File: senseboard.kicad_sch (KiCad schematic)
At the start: 73 parts, among them J1 Micro_SD_Card_Det1, J2 USB_C_Receptacle_USB2.0_16P, SW1 SW_Push, U1 STM32L4Q5CGUx, U2 SHT4x, U3 SCD41-D-R2, U4 SGP41-D-R4, U5 TPS62840DLCR, U6 TPS62840DLCR, U7 USBLC6-2SC6, U8 SGP41-D-R4, U9 RFM95W-915S2, Y1 Crystal_GND3

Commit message: added initial bom
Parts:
- U2: renamed from U6; footprint VSON8_2P1X1P6_TEX -> TPS62840DLCR:VSON8_2P1X1P6_TEX
- U3: renamed from U5; footprint VSON8_2P1X1P6_TEX -> TPS62840DLCR:VSON8_2P1X1P6_TEX
- renumbered C8 to C11, C11 to C12, C9 to C13, C7 to C14, C19 to C16, C20 to C17, C16 to C18, C21 to C19, C3 to C2, C22 to C20, C17 to C21, C23 to C22, C24 to C23, C18 to C24, C5 to C3, C13 to C4, C12 to C5, C2 to C6, C4 to C7, C14 to C8, C6 to C9, D3 to D1, D1 to D2, D4 to D3, D2 to D4, J2 to J1, J1 to J2, R2 to R1, R19 to R10, R20 to R11, R21 to R12, R5 to R13, R3 to R14, R22 to R15, R6 to R16, R7 to R17, R8 to R18, R9 to R19, R15 to R2, R10 to R20, R11 to R21, R12 to R22, R25 to R24, R24 to R25, R16 to R3, R13 to R4, R14 to R5, R1 to R6, R4 to R7, R17 to R8, R18 to R9, U7 to U1, U3 to U4, U4 to U5, U8 to U6, U2 to U7, U1 to U8

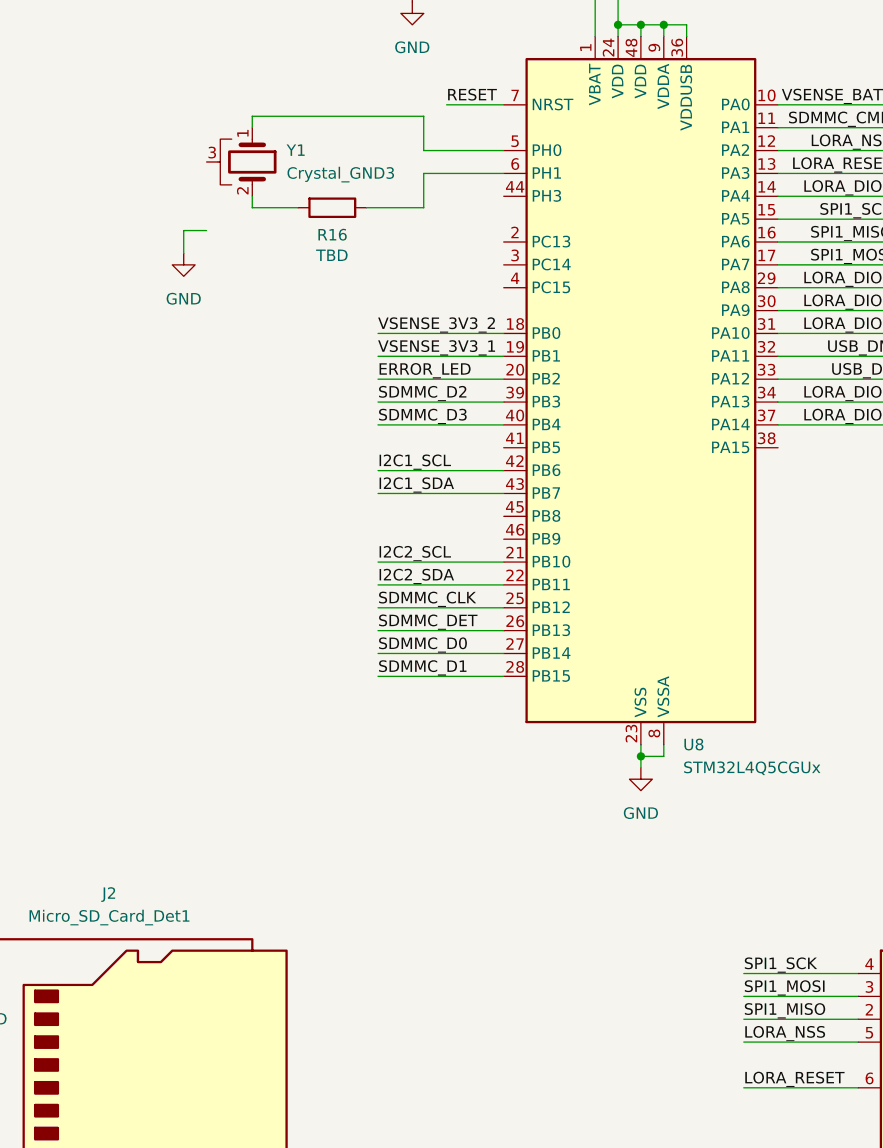
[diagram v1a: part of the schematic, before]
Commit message: fixed gnd positioning and added error led
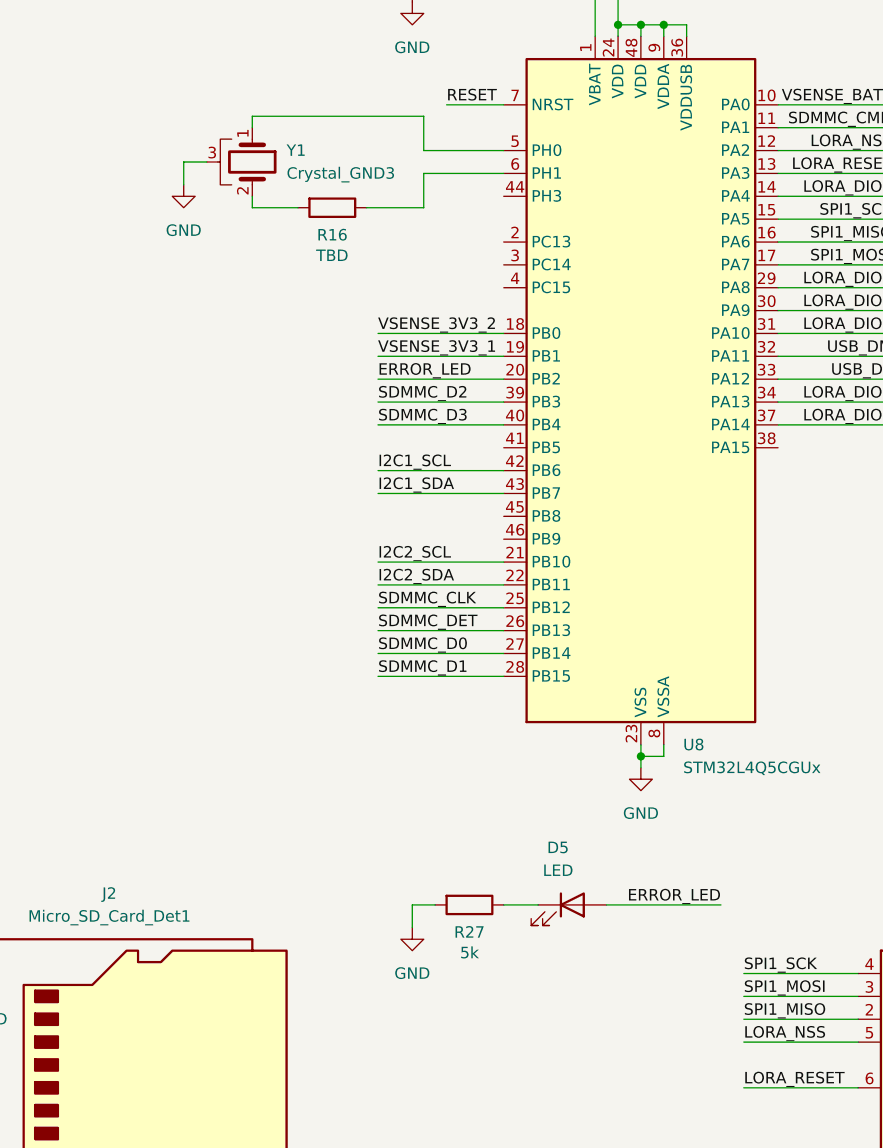
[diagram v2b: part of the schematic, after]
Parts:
- added D5: LED, symbol Device:LED
- added R27: 5k, symbol Device:R
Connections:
- net ERROR_LED: now also D5.2 (A)
- net GND: now also Y1.3, R27.2
- new net: D5.1 (K), R27.1

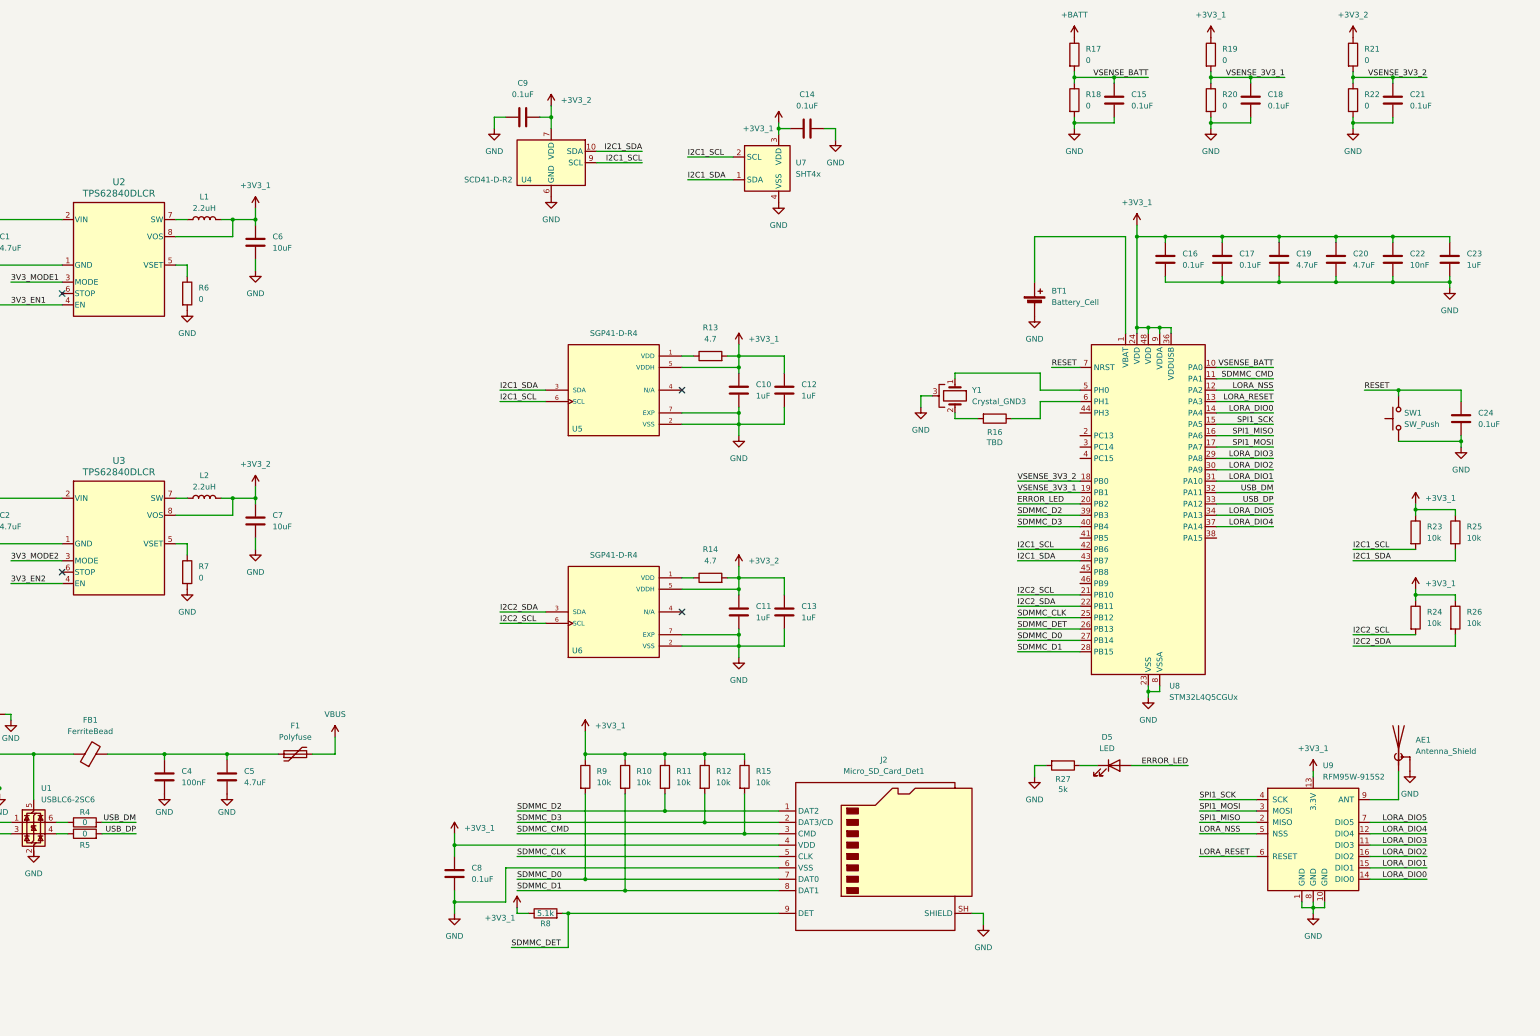
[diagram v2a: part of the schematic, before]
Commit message: minor changes to schematic, modified sd card holder and added all footprint references, began layout of board
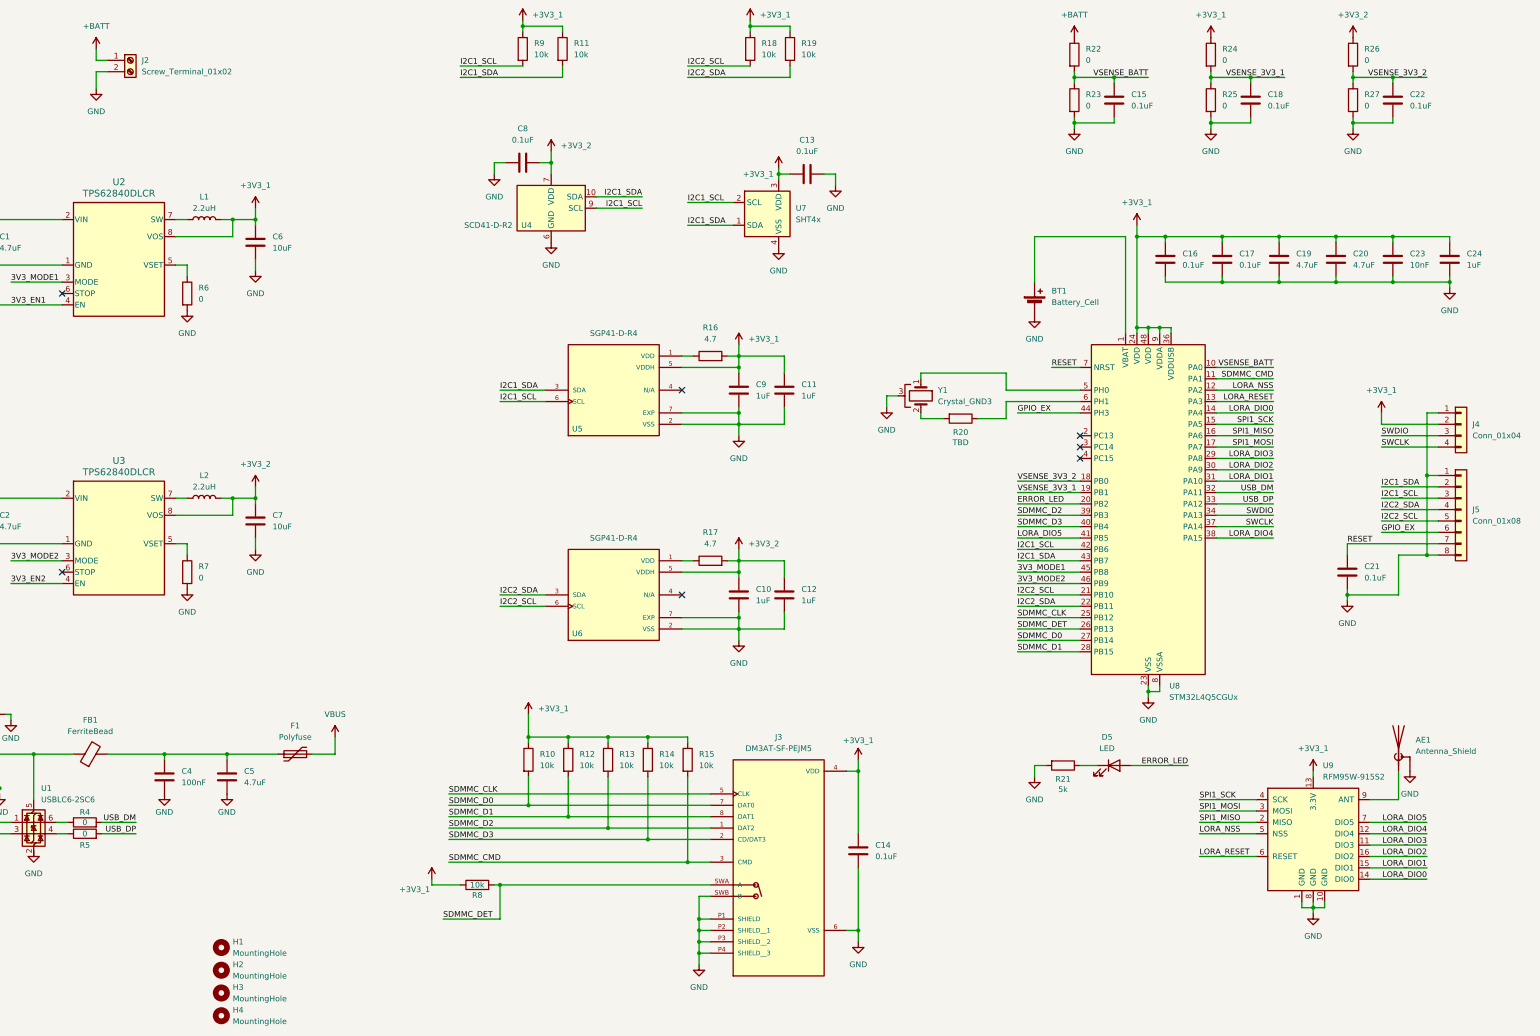
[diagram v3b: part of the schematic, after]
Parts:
- removed J2: Micro_SD_Card_Det1, symbol Connector:Micro_SD_Card_Det1
- removed SW1: SW_Push, symbol Switch:SW_Push
- added H1, H2, H3, H4: MountingHole, MountingHole:MountingHole_3.2mm_M3_ISO7380, symbol Mechanical:MountingHole
- added J2: Screw_Terminal_01x02, Connector_JST:JST_XH_B2B-XH-AM_1x02_P2.50mm_Vertical, symbol Connector:Screw_Terminal_01x02
- added J3: DM3AT-SF-PEJM5, DM3AT_SF_PEJM5:HRS_DM3AT-SF-PEJM5, symbol DM3AT-SF-PEJM5:DM3AT-SF-PEJM5
- added J4: Conn_01x04, Connector_PinHeader_2.54mm:PinHeader_1x04_P2.54mm_Vertical, symbol Connector_Generic:Conn_01x04
- added J5: Conn_01x08, Connector_PinHeader_2.54mm:PinHeader_1x08_P2.54mm_Vertical, symbol Connector_Generic:Conn_01x08
- AE1: footprint (none) -> Connector_Coaxial:SMA_Molex_73251-1153_EdgeMount_Horizontal
- BT1: footprint (none) -> Battery:BatteryHolder_Keystone_1057_1x2032
- C1, C19, C2, C20, C5, C6, C7: footprint (none) -> Capacitor_SMD:C_0805_2012Metric
- C10: renamed from C11; footprint (none) -> Capacitor_SMD:C_0603_1608Metric
- C11: renamed from C12; footprint (none) -> Capacitor_SMD:C_0603_1608Metric
- C12: renamed from C13; footprint (none) -> Capacitor_SMD:C_0603_1608Metric
- C13: renamed from C14; footprint (none) -> Capacitor_SMD:C_0402_1005Metric
- C14: renamed from C8; footprint (none) -> Capacitor_SMD:C_0402_1005Metric
- C15, C16, C17, C18, C3, C4: footprint (none) -> Capacitor_SMD:C_0402_1005Metric
- C21: renamed from C24; footprint (none) -> Capacitor_SMD:C_0402_1005Metric
- C22: renamed from C21; footprint (none) -> Capacitor_SMD:C_0402_1005Metric
- C23: renamed from C22; footprint (none) -> Capacitor_SMD:C_0402_1005Metric
- C24: renamed from C23; footprint (none) -> Capacitor_SMD:C_0603_1608Metric
- C8: renamed from C9; footprint (none) -> Capacitor_SMD:C_0402_1005Metric
- C9: renamed from C10; footprint (none) -> Capacitor_SMD:C_0603_1608Metric
- D1, D2, D3, D4: footprint (none) -> Diode_SMD:D_SMP_DO-220AA
- D5: footprint (none) -> LED_SMD:LED_0402_1005Metric
- F1: footprint (none) -> Fuse:Fuse_0805_2012Metric
- FB1: footprint (none) -> Inductor_SMD:L_0603_1608Metric
- J1: footprint (none) -> Connector_USB:USB_C_Receptacle_G-Switch_GT-USB-7010ASV
- L1, L2: footprint (none) -> Inductor_SMD:L_Murata_DFE201610P
- R1, R15, R2, R3, R4, R5, R6, R7: footprint (none) -> Resistor_SMD:R_0402_1005Metric
- R10: renamed from R9; footprint (none) -> Resistor_SMD:R_0402_1005Metric
- R11: renamed from R25; footprint (none) -> Resistor_SMD:R_0402_1005Metric
- R12: renamed from R10; footprint (none) -> Resistor_SMD:R_0402_1005Metric
- R13: renamed from R11; footprint (none) -> Resistor_SMD:R_0402_1005Metric
- R14: renamed from R12; footprint (none) -> Resistor_SMD:R_0402_1005Metric
- R16: renamed from R13; footprint (none) -> Resistor_SMD:R_0603_1608Metric
- R17: renamed from R14; footprint (none) -> Resistor_SMD:R_0603_1608Metric
- R18: renamed from R24; footprint (none) -> Resistor_SMD:R_0402_1005Metric
- R19: renamed from R26; footprint (none) -> Resistor_SMD:R_0402_1005Metric
- R20: renamed from R16; footprint (none) -> Resistor_SMD:R_0402_1005Metric
- R21: renamed from R27; footprint (none) -> Resistor_SMD:R_0402_1005Metric
- R22: renamed from R17; footprint (none) -> Resistor_SMD:R_0402_1005Metric
- R23: renamed from R18; footprint (none) -> Resistor_SMD:R_0402_1005Metric
- R24: renamed from R19; footprint (none) -> Resistor_SMD:R_0402_1005Metric
- R25: renamed from R20; footprint (none) -> Resistor_SMD:R_0402_1005Metric
- R26: renamed from R21; footprint (none) -> Resistor_SMD:R_0402_1005Metric
- R27: renamed from R22; footprint (none) -> Resistor_SMD:R_0402_1005Metric
- R8: value 5.1k -> 10k; footprint (none) -> Resistor_SMD:R_0402_1005Metric
- R9: renamed from R23; footprint (none) -> Resistor_SMD:R_0402_1005Metric
- U9: footprint (none) -> RF_Module:HOPERF_RFM9XW_SMD
- Y1: footprint (none) -> Crystal:Resonator_SMD_Murata_CSTxExxV-3Pin_3.0x1.1mm
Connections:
- net +3V3_1: now also C14.1, J3.4 (VDD), J4.2 (Pin_2); no longer C14.2
- net +BATT: now also J2.1 (Pin_1)
- net 3V3_MODE1: now also U8.45 (PB8)
- net 3V3_MODE2: now also U8.46 (PB9)
- net GND: now also C14.2, J2.2 (Pin_2), J3.6 (VSS), J3.P1 (SHIELD), J3.P2 (SHIELD__1), J3.P3 (SHIELD__2), J3.P4 (SHIELD__3), J3.SWB (B), J4.1 (Pin_1), J5.1 (Pin_1), J5.8 (Pin_8); no longer C14.1
- net I2C1_SCL: now also J5.3 (Pin_3)
- net I2C1_SDA: now also J5.2 (Pin_2)
- net I2C2_SCL: now also J5.5 (Pin_5)
- net I2C2_SDA: now also J5.4 (Pin_4)
- net LORA_DIO4: now also U8.38 (PA15); no longer U8.37 (PA14)
- net LORA_DIO5: now also U8.41 (PB5); no longer U8.34 (PA13)
- net RESET: now also J5.7 (Pin_7)
- net SDMMC_CLK: now also J3.5 (CLK)
- net SDMMC_CMD: now also J3.3 (CMD)
- net SDMMC_D0: now also J3.7 (DAT0)
- net SDMMC_D1: now also J3.8 (DAT1)
- net SDMMC_D2: now also J3.1 (DAT2)
- net SDMMC_D3: now also J3.2 (CD/DAT3)
- net SDMMC_DET: now also J3.SWA (A)
- net GPIO_EX: now reaches U8.44 (PH3)
- net GPIO_EX: now also J5.6 (Pin_6)
- new net SWCLK: J4.4 (Pin_4), U8.37 (PA14)
- new net SWDIO: J4.3 (Pin_3), U8.34 (PA13)
- no-connect marks 6 -> 9
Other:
- moved on the sheet: C10, C12, C13, C14, C21, C8, R10, R11, R12, R13, R14, R15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
